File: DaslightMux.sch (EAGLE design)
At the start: 11 parts, among them U1 XC9572XL, X1 B1-B24, X2 B25-B48

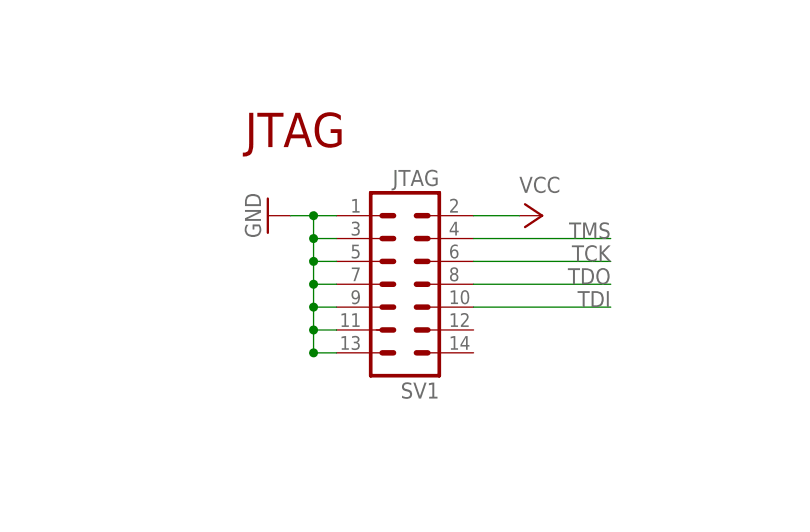
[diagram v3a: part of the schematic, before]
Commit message: Remodeled enclosure and adapted pcb layout
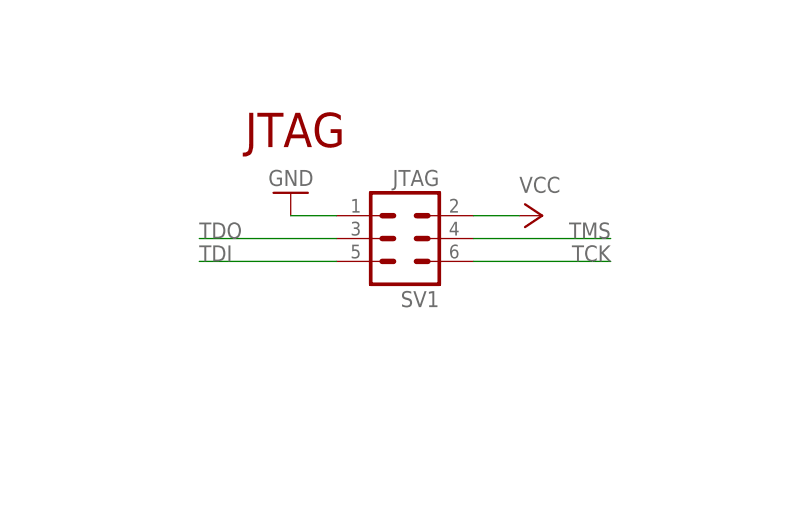
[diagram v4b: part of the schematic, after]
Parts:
- SV1: device con-harting-ml:ML14 -> con-lstb:MA03-2
- SV2: device con-harting-ml:ML10 -> con-harting-ml:ML10L
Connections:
- net GND: no longer SV1.11, SV1.13, SV1.3, SV1.5, SV1.7, SV1.9
- net TDI: now also SV1.5; no longer SV1.10
- net TDO: now also SV1.3; no longer SV1.8
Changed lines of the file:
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@@
 <part name="GND1" library="supply1" deviceset="GND" device=""/>
 <part name="P+1" library="supply1" deviceset="VCC" device=""/>
-<part name="SV1" library="con-harting-ml" deviceset="ML14" device="" value="JTAG"/>
 <part name="P+2" library="supply1" deviceset="VCC" device=""/>
 <part name="GND2" library="supply1" deviceset="GND" device=""/>
 <part name="P+3" library="supply1" deviceset="VCC" device=""/>
-<part name="SV2" library="con-harting-ml" deviceset="ML10" device="" value="HE10"/>
+<part name="SV2" library="con-harting-ml" deviceset="ML10" device="L" value="HE10"/>
 <part name="GND3" library="supply1" deviceset="GND" device=""/>
 <part name="C3" library="resistor" deviceset="C-EU" device="C0603" value="100n"/>
@@
 <part name="GND7" library="supply1" deviceset="GND" device=""/>
 <part name="C2" library="resistor" deviceset="C-EU" device="C0603" value="100n"/>
+<part name="SV1" library="con-lstb" deviceset="MA03-2" device="" value="JTAG"/>
 </parts>
 <sheets>
@@
 <instances>
 <instance part="U1" gate="G$1" x="66.04" y="86.36"/>
-<instance part="GND1" gate="1" x="142.24" y="60.96" rot="R270"/>
+<instance part="GND1" gate="1" x="144.78" y="63.5" rot="R180"/>
 <instance part="P+1" gate="VCC" x="172.72" y="60.96" rot="R270"/>
-<instance part="SV1" gate="1" x="157.48" y="53.34" rot="R180"/>
 <instance part="P+2" gate="VCC" x="111.76" y="109.22" rot="R270"/>
 <instance part="GND2" gate="1" x="111.76" y="127" rot="R90"/>
@@
 <instance part="GND7" gate="1" x="226.06" y="86.36"/>
 <instance part="C2" gate="G$1" x="167.64" y="99.06"/>
+<instance part="SV1" gate="1" x="157.48" y="58.42" rot="R180"/>
 </instances>
 <busses>
@@
 <net name="GND" class="0">
 <segment>
-<wire x1="149.86" y1="60.96" x2="147.32" y2="60.96" width="0.1524" layer="91"/>
-<wire x1="147.32" y1="60.96" x2="144.78" y2="60.96" width="0.1524" layer="91"/>
-<wire x1="149.86" y1="58.42" x2="147.32" y2="58.42" width="0.1524" layer="91"/>
-<wire x1="147.32" y1="58.42" x2="147.32" y2="60.96" width="0.1524" layer="91"/>
-<wire x1="149.86" y1="55.88" x2="147.32" y2="55.88" width="0.1524" layer="91"/>
-<wire x1="147.32" y1="55.88" x2="147.32" y2="58.42" width="0.1524" layer="91"/>
-<wire x1="149.86" y1="53.34" x2="147.32" y2="53.34" width="0.1524" layer="91"/>
-<wire x1="147.32" y1="53.34" x2="147.32" y2="55.88" width="0.1524" layer="91"/>
-<wire x1="149.86" y1="50.8" x2="147.32" y2="50.8" width="0.1524" layer="91"/>
-<wire x1="147.32" y1="50.8" x2="147.32" y2="53.34" width="0.1524" layer="91"/>
-<wire x1="149.86" y1="48.26" x2="147.32" y2="48.26" width="0.1524" layer="91"/>
-<wire x1="147.32" y1="48.26" x2="147.32" y2="50.8" width="0.1524" layer="91"/>
-<wire x1="149.86" y1="45.72" x2="147.32" y2="45.72" width="0.1524" layer="91"/>
-<wire x1="147.32" y1="45.72" x2="147.32" y2="48.26" width="0.1524" layer="91"/>
+<wire x1="149.86" y1="60.96" x2="144.78" y2="60.96" width="0.1524" layer="91"/>
 <pinref part="GND1" gate="1" pin="GND"/>
-<junction x="147.32" y="60.96"/>
-<junction x="147.32" y="58.42"/>
-<junction x="147.32" y="55.88"/>
-<junction x="147.32" y="53.34"/>
-<junction x="147.32" y="50.8"/>
-<junction x="147.32" y="48.26"/>
-<junction x="147.32" y="45.72"/>
 <pinref part="SV1" gate="1" pin="1"/>
-<pinref part="SV1" gate="1" pin="3"/>
-<pinref part="SV1" gate="1" pin="5"/>
-<pinref part="SV1" gate="1" pin="7"/>
-<pinref part="SV1" gate="1" pin="9"/>
-<pinref part="SV1" gate="1" pin="11"/>
-<pinref part="SV1" gate="1" pin="13"/>
 </segment>
 <segment>
@@
 <net name="TDO" class="0">
 <segment>
-<wire x1="165.1" y1="53.34" x2="180.34" y2="53.34" width="0.1524" layer="91"/>
-<label x="180.34" y="53.34" size="1.778" layer="95" rot="MR0"/>
-<pinref part="SV1" gate="1" pin="8"/>
+<wire x1="134.62" y1="58.42" x2="149.86" y2="58.42" width="0.1524" layer="91"/>
+<label x="134.62" y="58.42" size="1.778" layer="95"/>
+<pinref part="SV1" gate="1" pin="3"/>
 </segment>
 <segment>
@@
 <net name="TDI" class="0">
 <segment>
-<wire x1="180.34" y1="50.8" x2="165.1" y2="50.8" width="0.1524" layer="91"/>
-<label x="180.34" y="50.8" size="1.778" layer="95" rot="MR0"/>
-<pinref part="SV1" gate="1" pin="10"/>
+<wire x1="149.86" y1="55.88" x2="134.62" y2="55.88" width="0.1524" layer="91"/>
+<label x="134.62" y="55.88" size="1.778" layer="95"/>
+<pinref part="SV1" gate="1" pin="5"/>
 </segment>
 <segment>

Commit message: Ordered version of pcb
(added solder pads for pins 9-13)
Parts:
- added LSP10, LSP11, LSP12, LSP13, LSP9: LSP10, solpad:LSP10
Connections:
- new net N$11: LSP9.MP, U1.PB01_13
- new net N$12: LSP10.MP, U1.PB01_15
- new net N$13: LSP11.MP, U1.PB01_14
- new net N$14: LSP12.MP, U1.PB01_16
- new net N$15: LSP13.MP, U1.PB00_01
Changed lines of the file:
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@@
 <?xml version="1.0" encoding="utf-8"?>
 <!DOCTYPE eagle SYSTEM "eagle.dtd">
-<eagle version="6.4">
+<eagle version="6.5.0">
 <drawing>
 <settings>
@@
 <part name="C2" library="resistor" deviceset="C-EU" device="C0603" value="100n"/>
 <part name="SV1" library="con-lstb" deviceset="MA03-2" device="" value="JTAG"/>
+<part name="LSP9" library="solpad" deviceset="LSP10" device=""/>
+<part name="LSP10" library="solpad" deviceset="LSP10" device=""/>
+<part name="LSP11" library="solpad" deviceset="LSP10" device=""/>
+<part name="LSP12" library="solpad" deviceset="LSP10" device=""/>
+<part name="LSP13" library="solpad" deviceset="LSP10" device=""/>
 </parts>
 <sheets>
@@
 <instance part="C2" gate="G$1" x="167.64" y="99.06"/>
 <instance part="SV1" gate="1" x="157.48" y="58.42" rot="R180"/>
+<instance part="LSP9" gate="1" x="22.86" y="63.5" rot="R90"/>
+<instance part="LSP10" gate="1" x="17.78" y="58.42" rot="R90"/>
+<instance part="LSP11" gate="1" x="20.32" y="60.96" rot="R90"/>
+<instance part="LSP12" gate="1" x="15.24" y="55.88" rot="R90"/>
+<instance part="LSP13" gate="1" x="20.32" y="142.24" rot="R90"/>
 </instances>
 <busses>
@@
 </segment>
 </net>
+<net name="N$11" class="0">
+<segment>
+<pinref part="U1" gate="G$1" pin="PB01_13"/>
+<pinref part="LSP9" gate="1" pin="MP"/>
+<wire x1="25.4" y1="63.5" x2="35.56" y2="63.5" width="0.1524" layer="91"/>
+</segment>
+</net>
+<net name="N$12" class="0">
+<segment>
+<pinref part="U1" gate="G$1" pin="PB01_15"/>
+<pinref part="LSP10" gate="1" pin="MP"/>
+<wire x1="20.32" y1="58.42" x2="35.56" y2="58.42" width="0.1524" layer="91"/>
+</segment>
+</net>
+<net name="N$13" class="0">
+<segment>
+<pinref part="U1" gate="G$1" pin="PB01_14"/>
+<pinref part="LSP11" gate="1" pin="MP"/>
+<wire x1="22.86" y1="60.96" x2="35.56" y2="60.96" width="0.1524" layer="91"/>
+</segment>
+</net>
+<net name="N$14" class="0">
+<segment>
+<pinref part="U1" gate="G$1" pin="PB01_16"/>
+<pinref part="LSP12" gate="1" pin="MP"/>
+<wire x1="17.78" y1="55.88" x2="35.56" y2="55.88" width="0.1524" layer="91"/>
+</segment>
+</net>
+<net name="N$15" class="0">
+<segment>
+<pinref part="U1" gate="G$1" pin="PB00_01"/>
+<pinref part="LSP13" gate="1" pin="MP"/>
+<wire x1="22.86" y1="142.24" x2="35.56" y2="142.24" width="0.1524" layer="91"/>
+</segment>
+</net>
